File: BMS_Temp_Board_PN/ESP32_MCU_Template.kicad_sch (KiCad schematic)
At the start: 81 parts, among them IC1 ESP32-S3-WROOM-1-N8R8, IC10 CD74HC4067PWR, IC11 CD74HC4067PWR, IC12 CD74HC4067PWR, IC13 CD74HC4067PWR, IC14 CD74HC4067PWR, IC15 CD74HC4067PWR, IC16 CD74HC4067PWR, IC17 CD74HC4067PWR, IC18 CD74HC4067PWR, IC19 CD74HC4067PWR, IC2 CP2102N-A02-GQFN28, IC20 CD74HC4067PWR, IC21 CD74HC4067PWR, IC22 CD74HC4067PWR, IC23 CD74HC4067PWR, IC24 CD74HC4067PWR, IC3 TLP175A_TPL,E, IC4 TPS2116DRLR, IC5 MIC37100-3.3WS, IC6 CD74HC4067PWR, IC7 CD74HC4067PWR, IC8 CD74HC4067PWR, IC9 CD74HC4067PWR, J1 ESP_USB, J10 B32B-PUDSS-1_LF__SN_, J11 B32B-PUDSS-1_LF__SN_, J12 B32B-PUDSS-1_LF__SN_, J13 B32B-PUDSS-1_LF__SN_, J14 B32B-PUDSS-1_LF__SN_, J15 B32B-PUDSS-1_LF__SN_, J16 B32B-PUDSS-1_LF__SN_, J17 B32B-PUDSS-1_LF__SN_, J18 B32B-PUDSS-1_LF__SN_, J19 B32B-PUDSS-1_LF__SN_, J2 B32B-PUDSS-1_LF__SN_, J20 B32B-PUDSS-1_LF__SN_, J3 B32B-PUDSS-1_LF__SN_, J4 B32B-PUDSS-1_LF__SN_, J5 B32B-PUDSS-1_LF__SN_, J6 B32B-PUDSS-1_LF__SN_, J7 B32B-PUDSS-1_LF__SN_, J8 B32B-PUDSS-1_LF__SN_, J9 B32B-PUDSS-1_LF__SN_, Q1 MMBT2222LT1G, Q2 MMBT2222LT1G, U1 USBLC6-2SC6, U2 SN65HVD230

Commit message: Revised BMS Temperature Board and precharge circuit
the precharge circuit is a *very* basic schematic, not really finished
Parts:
- removed IC16, IC17, IC18, IC19, IC20, IC21, IC22, IC23, IC24: CD74HC4067PWR, CD74HC4067PWR:TSSOP24_4P5X7P9_TEX, symbol CD74HC4067PWR:CD74HC4067PWR
- removed J12, J13, J14, J15, J16, J17, J18, J19, J20: B32B-PUDSS-1_LF__SN_, Connector_JST:JST_PUD_B32B-PUDSS_2x16_P2.00mm_Vertical, symbol B32B-PUDSS-1_LF__SN_:B32B-PUDSS-1_LF__SN_
- added J12: B2B-PH-K-S, B2B_PH_K_S:JST_B2B-PH-K-S, symbol B2B-PH-K-S:B2B-PH-K-S
- added LED3: LED, LED_SMD:LED_0603_1608Metric, symbol Device:LED
- added R16: 220, Resistor_SMD:R_0603_1608Metric, symbol Device:R
- J10, J11, J2, J3, J4, J5, J6, J7, J8, J9: footprint Connector_JST:JST_PUD_B32B-PUDSS_2x16_P2.00mm_Vertical -> ESP32_S3_WROOM_1_N8R8:JST_PUD_B32B-PUDSS_2x16_P2.00mm_Vertical_PN
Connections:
- net MUX11 is gone; now on net MUX3: IC1.14 (IO20)
- net MUX12 is gone; now on net MUX4: IC1.15 (IO3)
- net MUX13 is gone; now on net MUX6: IC1.17 (IO9)
- net MUX14 is gone; now on net MUX7: IC1.18 (IO10)
- net MUX15 is gone; now on net MUX8: IC1.19 (IO11)
- net MUX16 is gone; now on net MUX9: IC1.20 (IO12)
- net MUX17 is gone; now on net MUX10: IC1.21 (IO13)
- net MUX18 is gone; now on net MUX_S0: IC1.22 (IO14)
- net CAN_CTX: now also IC1.29 (IO36); no longer IC1.24 (IO47)
- net CAN_RTX: now also IC1.30 (IO37); no longer IC1.25 (IO48)
- net CAN_TERM: now also IC1.31 (IO38); no longer IC1.16 (IO46)
- net GND: now also LED3.1 (K)
- net MUX1: now also IC1.12 (IO8); no longer IC1.4 (IO4)
- net MUX10: no longer IC1.13 (IO19)
- net MUX2: now also IC1.13 (IO19); no longer IC1.5 (IO5)
- net MUX3: no longer IC1.6 (IO6)
- net MUX4: no longer IC1.7 (IO7)
- net MUX5: now also IC1.16 (IO46); no longer IC1.8 (IO15)
- net MUX6: no longer IC1.9 (IO16)
- net MUX7: no longer IC1.10 (IO17)
- net MUX8: no longer IC1.11 (IO18)
- net MUX9: no longer IC1.12 (IO8)
- net MUX_S0: no longer IC1.30 (IO37)
- net MUX_S1: now also IC1.23 (IO21); no longer IC1.31 (IO38)
- net MUX_S2: now also IC1.24 (IO47); no longer IC1.32 (IO39)
- net MUX_S3: now also IC1.25 (IO48); no longer IC1.33 (IO40)
- net USER_LED: now also IC1.11 (IO18); no longer IC1.28 (IO35)
- net MUX19: no longer names the net of IC1.38 (IO2)
- new net: J12.2, R16.1
- new net: LED3.2 (A), R16.2
- new net SHUTOFF: IC1.6 (IO6), J12.1
- no-connect marks 25 -> 33
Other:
- note added: "LED should be red"
- note added: "Shutoff Signal Connector + Indicator"
- note removed: "Move anywhere u want ^"

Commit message: (hopefully) final revision of the bms temp board
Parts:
- added H1, H2, H3, H4: MountingHole, MountingHole:MountingHole_2.2mm_M2, symbol Mechanical:MountingHole
- added J13: SM04B-ULHK-1TA1-ETB_HF_, SM04B-ULH:SM04BULHK1TA1ETBHF, symbol SM04B-ULHK-1TA1-ETB_HF_:SM04B-ULHK-1TA1-ETB_HF_
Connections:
- net +5V: now also J13.4
- net CAN+: now also J13.2
- net CAN-: now also J13.3
- net GND: now also J13.1
- no-connect marks 33 -> 35

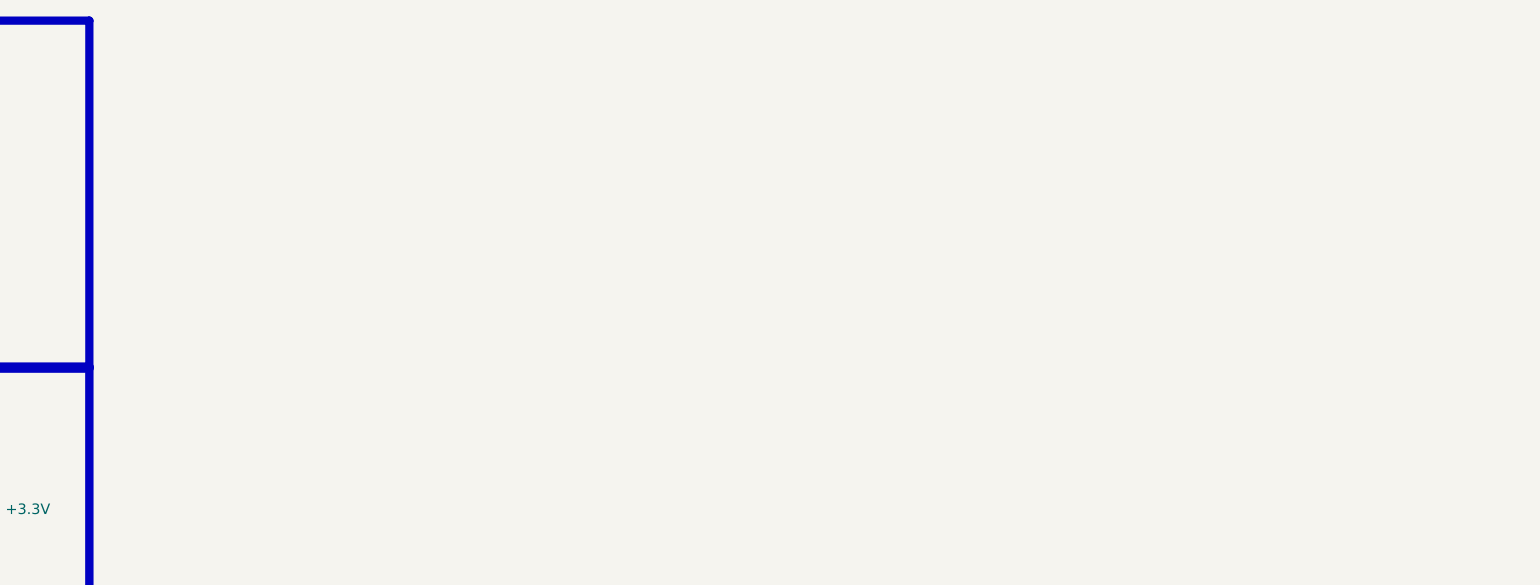
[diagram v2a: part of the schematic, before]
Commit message: Reviewing Board
Ready for DAQ Review
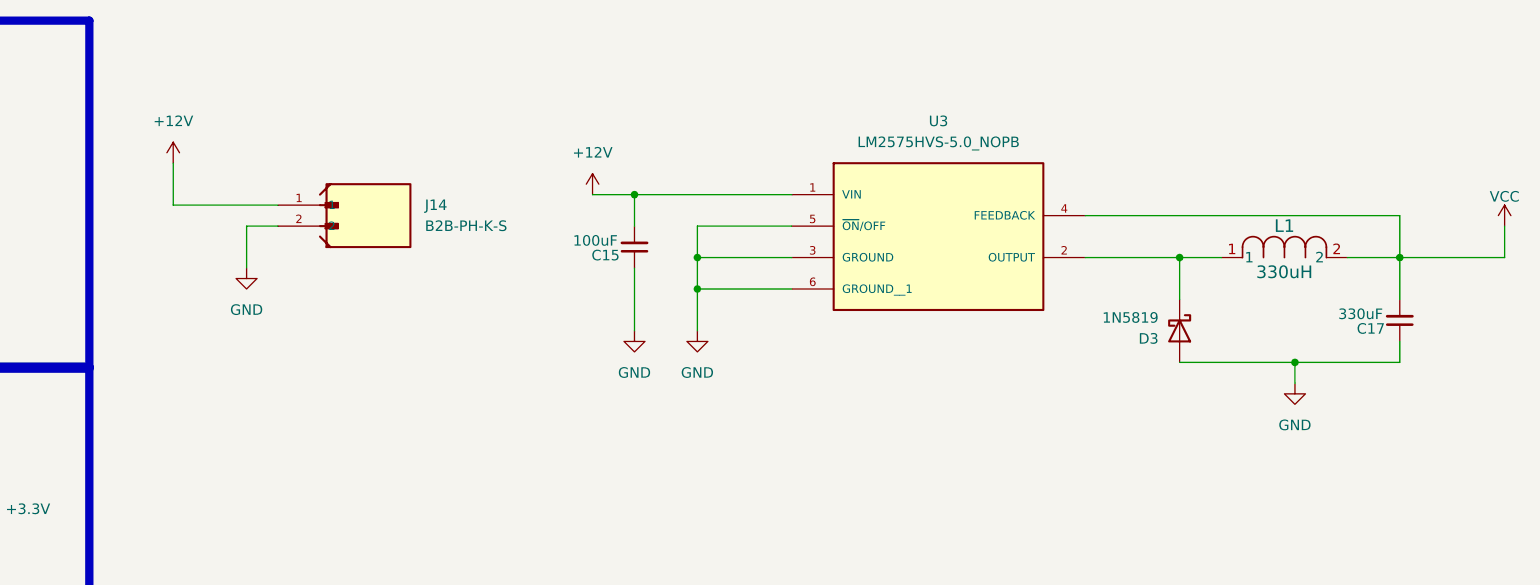
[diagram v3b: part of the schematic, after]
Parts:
- added C15: 100uF, Capacitor_SMD:C_0603_1608Metric, symbol Device:C_Small
- added C17: 330uF, Capacitor_SMD:C_0603_1608Metric, symbol Device:C_Small
- added D3: 1N5819, Diode_THT:D_DO-41_SOD81_P10.16mm_Horizontal, symbol Diode:1N5819
- added J14: B2B-PH-K-S, B2B_PH_K_S:JST_B2B-PH-K-S, symbol B2B-PH-K-S:B2B-PH-K-S
- added L1: 330uH, Nadine:IND_SPD127R_API, symbol BMS Tempboard:SPD127R-334M
- added U3: LM2575HVS-5.0_NOPB, Nadine:VREG_LM2575HVS-5.0_NOPB, symbol BMS Tempboard:LM2575HVS-5.0_NOPB
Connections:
- net GND: now also C15.1, C17.1, D3.2 (A), J14.2, U3.3 (GROUND), U3.5 (~{ON}/OFF), U3.6 (GROUND__1)
- net VCC: now also C17.2, L1.2, U3.4 (FEEDBACK)
- new net: D3.1 (K), L1.1, U3.2 (OUTPUT)
- new net +12V: C15.2, J14.1, U3.1 (VIN)
